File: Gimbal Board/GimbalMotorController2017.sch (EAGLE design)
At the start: 122 parts, among them J1 SL03THROUGH_HOLE, J3 APP_2POS_CONFIG5V_HORIZ, Q7 MOSFET-PCHANNEL, Q8 MOSFET-PCHANNEL, Q9 MOSFET-NCHANNELAO3404A, U1 NUP4201MR6, U2 MAX3232D, U3 CSD18533Q5A, U4 CSD18533Q5A, U5 CSD18533Q5A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

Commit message: Added new FET package, reorganized schematic to further clean up the labeling
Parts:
- removed U3, U4, U5, U6, U7, U8: CSD18533Q5A, CSD18533:CSD18533Q5A
- added Q1, Q2, Q3, Q4, Q5, Q6: Q_IRF7437SMD, R6020ENJTL ROHM D2PACK:Q_IRF7437SMD
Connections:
- net GND: now also Q6.S; no longer U4.S
- net N$13: now also Q2.G; no longer U8.G
- net N$14: now also Q3.G; no longer U6.G
- net N$15: now also Q4.G; no longer U5.G
- net N$16: now also Q1.G; no longer U7.G
- net N$17: now also Q5.G; no longer U3.G
- net N$18: now also Q6.G; no longer U4.G
- net PVDD: now also Q2.D, Q3.D, Q5.D; no longer U3.D, U6.D, U8.D
- net SH_A: now also Q1.D, Q2.S; no longer U7.D, U8.S
- net SH_B: now also Q3.S, Q4.D; no longer U5.D, U6.S
- net SH_C: now also Q5.S, Q6.D; no longer U3.S, U4.D
- net SL_A: now also Q1.S; no longer U7.S
- net SL_B: now also Q4.S; no longer U5.S
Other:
- moved on the sheet: C19, C20, C21, C22, C23, C24, C25, C26, C44, C45, C46, C47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

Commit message: Updated resistor values to give 3.2v/15v ratio with resistors known to be available on digikey with the 0805 package
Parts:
- R14, R19, R24, R26: value 184k -> 191k
- R15, R20, R25, R27: value 50k -> 51.7k
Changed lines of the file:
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@@
 <?xml version="1.0" encoding="utf-8"?>
 <!DOCTYPE eagle SYSTEM "eagle.dtd">
-<eagle version="8.5.2">
+<eagle version="8.3.2">
 <drawing>
 <settings>
@@
 <part name="GND13" library="SparkFun-Aesthetics" library_urn="urn:adsk.eagle:library:507" deviceset="GND" device=""/>
 <part name="GND14" library="SparkFun-Aesthetics" library_urn="urn:adsk.eagle:library:507" deviceset="GND" device=""/>
-<part name="R14" library="SparkFun-Passives" deviceset="RESISTOR" device="0805-RES" value="184k"/>
-<part name="R15" library="SparkFun-Passives" deviceset="RESISTOR" device="0805-RES" value="50k"/>
+<part name="R14" library="SparkFun-Passives" deviceset="RESISTOR" device="0805-RES" value="191k"/>
+<part name="R15" library="SparkFun-Passives" deviceset="RESISTOR" device="0805-RES" value="51.7k"/>
 <part name="C20" library="SparkFun-Passives" deviceset="CAP" device="0805" value="0.1u"/>
 <part name="GND15" library="SparkFun-Aesthetics" library_urn="urn:adsk.eagle:library:507" deviceset="GND" device=""/>
@@
 <part name="GND16" library="SparkFun-Aesthetics" library_urn="urn:adsk.eagle:library:507" deviceset="GND" device=""/>
 <part name="GND17" library="SparkFun-Aesthetics" library_urn="urn:adsk.eagle:library:507" deviceset="GND" device=""/>
-<part name="R19" library="SparkFun-Passives" deviceset="RESISTOR" device="0805-RES" value="184k"/>
-<part name="R20" library="SparkFun-Passives" deviceset="RESISTOR" device="0805-RES" value="50k"/>
+<part name="R19" library="SparkFun-Passives" deviceset="RESISTOR" device="0805-RES" value="191k"/>
+<part name="R20" library="SparkFun-Passives" deviceset="RESISTOR" device="0805-RES" value="51.7k"/>
 <part name="C23" library="SparkFun-Passives" deviceset="CAP" device="0805" value="0.1u"/>
 <part name="GND18" library="SparkFun-Aesthetics" library_urn="urn:adsk.eagle:library:507" deviceset="GND" device=""/>
@@
 <part name="GND19" library="SparkFun-Aesthetics" library_urn="urn:adsk.eagle:library:507" deviceset="GND" device=""/>
 <part name="GND20" library="SparkFun-Aesthetics" library_urn="urn:adsk.eagle:library:507" deviceset="GND" device=""/>
-<part name="R24" library="SparkFun-Passives" deviceset="RESISTOR" device="0805-RES" value="184k"/>
-<part name="R25" library="SparkFun-Passives" deviceset="RESISTOR" device="0805-RES" value="50k"/>
+<part name="R24" library="SparkFun-Passives" deviceset="RESISTOR" device="0805-RES" value="191k"/>
+<part name="R25" library="SparkFun-Passives" deviceset="RESISTOR" device="0805-RES" value="51.7k"/>
 <part name="C26" library="SparkFun-Passives" deviceset="CAP" device="0805" value="0.1u"/>
 <part name="GND21" library="SparkFun-Aesthetics" library_urn="urn:adsk.eagle:library:507" deviceset="GND" device=""/>
@@
 <part name="C30" library="SparkFun-Passives" deviceset="CAP" device="0805" value="0.01u"/>
 <part name="R23" library="SparkFun-Passives" deviceset="RESISTOR" device="0805-RES" value="3.3"/>
-<part name="R26" library="SparkFun-Passives" deviceset="RESISTOR" device="0805-RES" value="184k"/>
-<part name="R27" library="SparkFun-Passives" deviceset="RESISTOR" device="0805-RES" value="50k"/>
+<part name="R26" library="SparkFun-Passives" deviceset="RESISTOR" device="0805-RES" value="191k"/>
+<part name="R27" library="SparkFun-Passives" deviceset="RESISTOR" device="0805-RES" value="51.7k"/>
 <part name="C31" library="SparkFun-Passives" deviceset="CAP" device="0805" value="0.1u"/>
 <part name="GND22" library="SparkFun-Aesthetics" library_urn="urn:adsk.eagle:library:507" deviceset="GND" device=""/>

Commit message: Updated resistor values for new divider, updated indicators section, changed PWM_IN_NO_FILTER to PWM_IN and removed previous PWM_IN label
Resistor values updated for 12v to 3.2v ratio. Simplified D6 indicator schematic to be just an LED, resistor, power, and ground. Changed old PWM_IN_NO_FILTER label to PWM_IN in external connections, and removed old PWM_IN label from PA2 pin in external connections.
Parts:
- removed D16: 15V, SparkFun-DiscreteSemi:DIODE-ZENER3.3V
- removed Q9: MOSFET-NCHANNELAO3404A, SparkFun-DiscreteSemi:MOSFET-NCHANNELAO3404A
- removed R50: 3M, SparkFun-Passives:RESISTOR0805-RES
- removed R51: 1M, SparkFun-Passives:RESISTOR0805-RES
- Q1, Q2, Q3, Q4, Q5, Q6: value Q_IRF7437SMD -> R6020ENJSMD; device R6020ENJTL ROHM D2PACK:Q_IRF7437SMD -> R6020ENJTL ROHM D2PACK:R6020ENJSMD
- R14, R19, R24, R26: value 191k -> 187k
- R15, R20, R25, R27: value 51.7k -> 68.1k
- R32: value 330 -> 1.2k
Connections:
- removed net N$36: C15.+
- removed net N$38: D16.C, Q9.G, R50.2, R51.1
- removed net N$41: D16.A, D6.A, Q9.S
- removed net PWM_IN_NO_FILTER: J1.3, U$2.PF4
- net GND: no longer R51.2
- net PVDD: now also C15.+, D6.A; no longer R50.1
- net PWM_IN: now also J1.3, U$2.PF4; no longer U$2.PA2
- net VCC: no longer Q9.D
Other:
- moved on the sheet: D6, D7, D8, D9, Q7, Q8, R32, R33, R34, R35

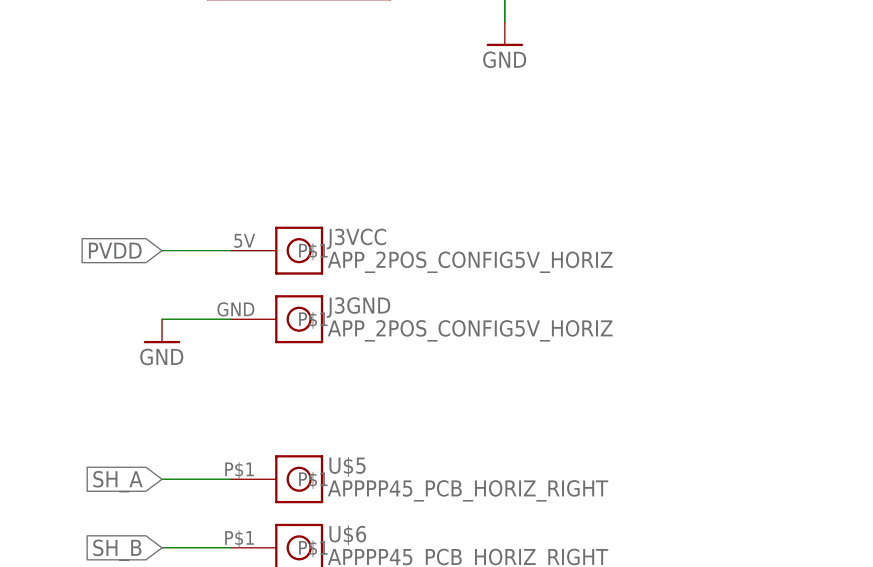
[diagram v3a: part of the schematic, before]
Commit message: Board routing was cleaned up. Silkscreen was cleaned up. Correct Package for Power Anderson Connectors is now being used.
Mounting holes were removed.  SL connectors were labelled. All test points are correctly named. More vias have been added to stitch the planes together. Traces were redrawn in many places for cleaner paths. Correct Vertical mounting board has been added. Anderson Power Package was changed to correct package. The inductor was moved to reduce noise. The power conditioning capacitor was moved out from under where the control card sits.
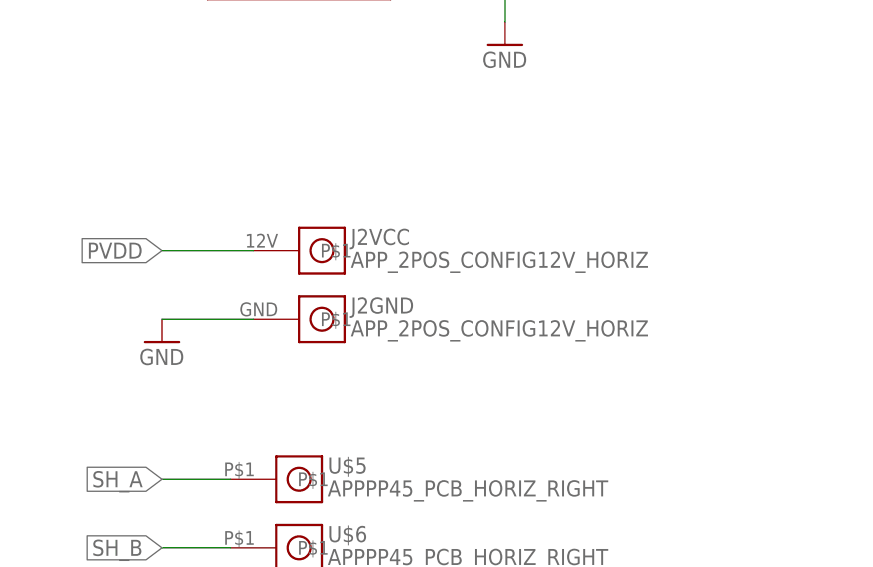
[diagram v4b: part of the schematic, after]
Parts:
- removed J3: APP_2POS_CONFIG5V_HORIZ, MRDT-Connectors:APP_2POS_CONFIG5V_HORIZ
- added J2: APP_2POS_CONFIG12V_HORIZ, MRDT-Connectors:APP_2POS_CONFIG12V_HORIZ
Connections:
- net GND: now also J2GND.P$1; no longer J3GND.P$1
- net PVDD: now also J2VCC.P$1; no longer J3VCC.P$1
